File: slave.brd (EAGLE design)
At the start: 321.3 x 281.9 mm, 324 parts, among them J2 EB21A-06-D, J3 EB21A-06-D, J4 EB21A-06-D, J5 EB21A-06-D, J6 282837-9, J7 282837-9, J8 282837-9, J9 1715250000, Q1 DMN2056U-7, Q10 DMN2056U-7, Q11 DMN2056U-7, Q12 DMN2056U-7, Q13 DMN2056U-7, Q14 DMN2056U-7, Q15 DMN2056U-7, Q16 DMN2056U-7, Q17 DMN2056U-7, Q18 DMN2056U-7, Q19 DMN2056U-7, Q2 DMN2056U-7, Q20 DMN2056U-7, Q21 DMN2056U-7, Q22 DMN2056U-7, Q23 DMN2056U-7, Q24 DMN2056U-7, Q25 DMN2056U-7, Q26 DMN2056U-7, Q27 DMN2056U-7, Q28 DMN2056U-7, Q29 DMN2056U-7, Q3 DMN2056U-7, Q30 DMN2056U-7, Q31 DMN2056U-7, Q32 DMN2056U-7, Q33 DMN2056U-7, Q34 DMN2056U-7, Q35 DMN2056U-7, Q36 DMN2056U-7, Q37 DMN2056U-7, Q38 DMN2056U-7, Q39 DMN2056U-7, Q4 DMN2056U-7, Q40 DMN2056U-7, Q41 DMN2056U-7, Q42 DMN2056U-7, Q5 DMN2056U-7, Q6 DMG2301L-7, Q7 DMN2056U-7, Q8 DMN2056U-7, Q9 DMN2056U-7, U2 AP2112K-3.3TRG1, U3 MCP23008-E/P, U4 MCP23008-E/P, U5 MCP23008-E/P, U6 MC74HCT4851ADR2G, U7 MC74HCT4851ADR2G, U8 MC74HCT4851ADR2G, U9 MC74HCT4851ADR2G

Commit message: removed backup files, finalized board layoout
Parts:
- removed D10, D8, D9: B5819W SL, ML_library:DIODE_SOD-123
- removed PR_CS1, PR_CS10, PR_CS11, PR_CS12, PR_CS13, PR_CS14, PR_CS15, PR_CS16, PR_CS17, PR_CS18, PR_CS19, PR_CS2, PR_CS20, PR_CS3, PR_CS4, PR_CS5, PR_CS6, PR_CS7, PR_CS8, PR_CS9: ACS723LLCTR-10AU-T, ACS723LLCTR-10AU-T:SOIC127P600X175-8N
- removed Q6: DMG2301L-7, ML_library:SOT23
- removed R32: 1k, OPL_Resistor:R0402
- removed R33: 10k, OPL_Resistor:R0402
- removed U$1, U$2: PPTC151LFBN-RC, PPTC151LFBN-RC:PPTC151LFBN-RC
- added ESP_LEFT_HDR, ESP_RIGHT_HDR: PPTC151LFBN-RC, PPTC151LFBN-RC:PPTC151LFBN-RC
- added OA_CS, OGF_CS, OGL_CS, OGR_CS, OR_CS, PA_CS, PGF_CS, PGL_CS, PGR_CS, PR_CS, SA_CS, SGF_CS, SGL_CS, SGR_CS, SPA_CS, SPGF_CS, SPGL_CS, SPGR_CS, SPR_CS, SR_CS: ACS723LLCTR-10AU-T, ACS723LLCTR-10AU-T:SOIC127P600X175-8N
- moved CB39 298.0 mm to (-240.1, 39.6), turned to 270 degrees
- moved R55 279.9 mm to (-203.3, 24.4), turned to 180 degrees
- moved CB36 279.3 mm to (-58.8, 41.5), turned to 90 degrees
- moved CB38 279.3 mm to (-69.0, 41.5), turned to 90 degrees
- moved R52 279.2 mm to (-186.8, 24.4), turned to 180 degrees
- moved CB35 278.4 mm to (-55.0, 41.5), turned to 270 degrees
- moved CB37 278.4 mm to (-65.2, 41.5), turned to 270 degrees
- moved R58 276.3 mm to (-212.2, 24.4), turned to 180 degrees
- moved R57 275.6 mm to (-205.8, 24.4)
- moved R54 274.9 mm to (-189.3, 24.4)
- moved R56 274.6 mm to (-204.6, 28.2), turned to 90 degrees
- moved R53 273.9 mm to (-188.1, 28.2), turned to 90 degrees
- moved R61 272.8 mm to (-221.1, 24.4), turned to 180 degrees
- moved R60 272.2 mm to (-214.7, 24.4)
- moved R59 271.0 mm to (-213.5, 28.2), turned to 90 degrees
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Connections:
- removed net 3V3_F: Q6.P$3
- removed net N$10: D8.2, D9.2, R32.1
- removed net N$35: CB9.1, PR_CS5.5
- removed net N$47: CB21.1, PR_CS11.5
- removed net N$5: D10.2, Q6.P$2
- removed net N$59: CB33.1, PR_CS17.5
- removed net N$65: CB39.1, PR_CS20.5
- removed net PMOS_G: Q6.P$1, R32.2, R33.2
- removed net VBAT: D9.1
- removed net VUSB: D8.1
- new net N$13: CB9.1, PGR_CS.5
- new net N$14: CB21.1, SGR_CS.5
- new net N$16: CB33.1, OGR_CS.5
- new net N$17: CB39.1, SPGR_CS.5
- net +5V: now also OA_CS.6, OA_CS.8, OGF_CS.6, OGF_CS.8, OGL_CS.6, OGL_CS.8, OGR_CS.6, OGR_CS.8, OR_CS.6, OR_CS.8, PA_CS.6, PA_CS.8, PGF_CS.6, PGF_CS.8, PGL_CS.6, PGL_CS.8, PGR_CS.6, PGR_CS.8, PR_CS.6, PR_CS.8, SA_CS.6, SA_CS.8, SGF_CS.6, SGF_CS.8, SGL_CS.6, SGL_CS.8, SGR_CS.6, SGR_CS.8, SPA_CS.6, SPA_CS.8, SPGF_CS.6, SPGF_CS.8, SPGL_CS.6, SPGL_CS.8, SPGR_CS.6, SPGR_CS.8, SPR_CS.6, SPR_CS.8, SR_CS.6, SR_CS.8; no longer PR_CS1.6, PR_CS1.8, PR_CS10.6, PR_CS10.8, PR_CS11.6, PR_CS11.8, PR_CS12.6, PR_CS12.8, PR_CS13.6, PR_CS13.8, PR_CS14.6, PR_CS14.8, PR_CS15.6, PR_CS15.8, PR_CS16.6, PR_CS16.8, PR_CS17.6, PR_CS17.8, PR_CS18.6, PR_CS18.8, PR_CS19.6, PR_CS19.8, PR_CS2.6, PR_CS2.8, PR_CS20.6, PR_CS20.8, PR_CS3.6, PR_CS3.8, PR_CS4.6, PR_CS4.8, PR_CS5.6, PR_CS5.8, PR_CS6.6, PR_CS6.8, PR_CS7.6, PR_CS7.8, PR_CS8.6, PR_CS8.8, PR_CS9.6, PR_CS9.8
- net 3V3: now also ESP_RIGHT_HDR.P$15; no longer D10.1, U$2.P$15
- net CS_SEL0: now also ESP_RIGHT_HDR.P$6; no longer U$2.P$6
- net CS_SEL1: now also ESP_RIGHT_HDR.P$4; no longer U$2.P$4
- net CS_SEL2: now also ESP_RIGHT_HDR.P$3; no longer U$2.P$3
- net D23: now also ESP_RIGHT_HDR.P$1; no longer U$2.P$1
- net EN: now also ESP_LEFT_HDR.P$1; no longer U$1.P$1
- net GND: now also ESP_LEFT_HDR.P$14, ESP_RIGHT_HDR.P$14; no longer R33.1, U$1.P$14, U$2.P$14
- net I_OA: now also OA_CS.7; no longer PR_CS8.7
- net I_OGF: now also OGF_CS.7; no longer PR_CS9.7
- net I_OGL: now also OGL_CS.7; no longer PR_CS10.7
- net I_OGR: now also OGR_CS.7; no longer PR_CS11.7
- net I_OR: now also OR_CS.7; no longer PR_CS7.7
- net I_PA: now also PA_CS.7; no longer PR_CS12.7
- net I_PGF: now also PGF_CS.7; no longer PR_CS18.7
- net I_PGL: now also PGL_CS.7; no longer PR_CS19.7
- net I_PGR: now also PGR_CS.7; no longer PR_CS20.7
- net I_PR: now also PR_CS.7; no longer PR_CS6.7
- net I_SA: now also SA_CS.7; no longer PR_CS2.7
- net I_SGF: now also SGF_CS.7; no longer PR_CS3.7
- net I_SGL: now also SGL_CS.7; no longer PR_CS4.7
- net I_SGR: now also SGR_CS.7; no longer PR_CS5.7
- net I_SPA: now also SPA_CS.7; no longer PR_CS14.7
- net I_SPGF: now also SPGF_CS.7; no longer PR_CS15.7
- net I_SPGL: now also SPGL_CS.7; no longer PR_CS16.7
- net I_SPGR: now also SPGR_CS.7; no longer PR_CS17.7
- net I_SPR: now also SPR_CS.7; no longer PR_CS13.7
- net I_SR: now also SR_CS.7; no longer PR_CS1.7
- net N$29: now also SR_CS.5; no longer PR_CS1.5
- net N$31: now also SA_CS.5; no longer PR_CS2.5
- net N$33: now also SGF_CS.5; no longer PR_CS3.5
- net N$37: now also PR_CS.5; no longer PR_CS6.5
- net N$39: now also OR_CS.5; no longer PR_CS7.5
- net N$4: now also SGL_CS.5; no longer PR_CS4.5
- net N$41: now also OA_CS.5; no longer PR_CS8.5
- net N$43: now also OGF_CS.5; no longer PR_CS9.5
- net N$45: now also OGL_CS.5; no longer PR_CS10.5
- net N$49: now also PA_CS.5; no longer PR_CS12.5
- net N$51: now also SPR_CS.5; no longer PR_CS13.5
- net N$53: now also SPA_CS.5; no longer PR_CS14.5
- net N$55: now also SPGF_CS.5; no longer PR_CS15.5
- net N$57: now also SPGL_CS.5; no longer PR_CS16.5
- net N$61: now also PGF_CS.5; no longer PR_CS18.5
- net N$63: now also PGL_CS.5; no longer PR_CS19.5
- net OA_IP-: now also OA_CS.3, OA_CS.4; no longer PR_CS8.3, PR_CS8.4
- net OGF_IP-: now also OGF_CS.3, OGF_CS.4; no longer PR_CS9.3, PR_CS9.4
- net OGL_IP-: now also OGL_CS.3, OGL_CS.4; no longer PR_CS10.3, PR_CS10.4
- net OGR_IP-: now also OGR_CS.3, OGR_CS.4; no longer PR_CS11.3, PR_CS11.4
- net OR_IP-: now also OR_CS.3, OR_CS.4; no longer PR_CS7.3, PR_CS7.4
- net O_CURRENT: now also ESP_LEFT_HDR.P$5; no longer U$1.P$5
- net PA: now also ESP_LEFT_HDR.P$12; no longer U$1.P$12
- net PA_IP-: now also PA_CS.3, PA_CS.4; no longer PR_CS12.3, PR_CS12.4
- net PGF: now also ESP_LEFT_HDR.P$11; no longer U$1.P$11
- net PGF_IP-: now also PGF_CS.3, PGF_CS.4; no longer PR_CS18.3, PR_CS18.4
- net PGL: now also ESP_LEFT_HDR.P$10; no longer U$1.P$10
- net PGL_IP-: now also PGL_CS.3, PGL_CS.4; no longer PR_CS19.3, PR_CS19.4
- net PGR: now also ESP_LEFT_HDR.P$9; no longer U$1.P$9
- net PGR_IP-: now also PGR_CS.3, PGR_CS.4; no longer PR_CS20.3, PR_CS20.4
- net PR: now also ESP_LEFT_HDR.P$13; no longer U$1.P$13
- net PR_IP-: now also PR_CS.3, PR_CS.4; no longer PR_CS6.3, PR_CS6.4
- net P_CURRENT: now also ESP_LEFT_HDR.P$7; no longer U$1.P$7
- net SA: now also ESP_LEFT_HDR.P$3; no longer U$1.P$3
- net SA_IP-: now also SA_CS.3, SA_CS.4; no longer PR_CS2.3, PR_CS2.4
- net SCL: now also ESP_RIGHT_HDR.P$2; no longer U$2.P$2
- net SDA: now also ESP_RIGHT_HDR.P$5; no longer U$2.P$5
- net SGF: now also ESP_LEFT_HDR.P$2; no longer U$1.P$2
- net SGF_IP-: now also SGF_CS.3, SGF_CS.4; no longer PR_CS3.3, PR_CS3.4
- net SGL: now also ESP_RIGHT_HDR.P$13; no longer U$2.P$13
- net SGL_IP-: now also SGL_CS.3, SGL_CS.4; no longer PR_CS4.3, PR_CS4.4
- net SGR: now also ESP_RIGHT_HDR.P$12; no longer U$2.P$12
- net SGR_IP-: now also SGR_CS.3, SGR_CS.4; no longer PR_CS5.3, PR_CS5.4
- net SPA: now also ESP_RIGHT_HDR.P$10; no longer U$2.P$10
- net SPA_IP-: now also SPA_CS.3, SPA_CS.4; no longer PR_CS14.3, PR_CS14.4
- net SPGF: now also ESP_RIGHT_HDR.P$9; no longer U$2.P$9
- net SPGF_IP-: now also SPGF_CS.3, SPGF_CS.4; no longer PR_CS15.3, PR_CS15.4
- net SPGL: now also ESP_RIGHT_HDR.P$8; no longer U$2.P$8
- net SPGL_IP-: now also SPGL_CS.3, SPGL_CS.4; no longer PR_CS16.3, PR_CS16.4
- net SPGR: now also ESP_RIGHT_HDR.P$7; no longer U$2.P$7
- net SPGR_IP-: now also SPGR_CS.3, SPGR_CS.4; no longer PR_CS17.3, PR_CS17.4
- net SPR: now also ESP_RIGHT_HDR.P$11; no longer U$2.P$11
- net SPR_IP-: now also SPR_CS.3, SPR_CS.4; no longer PR_CS13.3, PR_CS13.4
- net SP_CURRENT: now also ESP_LEFT_HDR.P$4; no longer U$1.P$4
- net SR: now also ESP_LEFT_HDR.P$8; no longer U$1.P$8
- net SR_IP-: now also SR_CS.3, SR_CS.4; no longer PR_CS1.3, PR_CS1.4
- net S_CURRENT: now also ESP_LEFT_HDR.P$6; no longer U$1.P$6
- net VIN: now also OA_CS.1, OA_CS.2, OGF_CS.1, OGF_CS.2, OGL_CS.1, OGL_CS.2, OGR_CS.1, OGR_CS.2, OR_CS.1, OR_CS.2, PA_CS.1, PA_CS.2, PGF_CS.1, PGF_CS.2, PGL_CS.1, PGL_CS.2, PGR_CS.1, PGR_CS.2, PR_CS.1, PR_CS.2, SA_CS.1, SA_CS.2, SGF_CS.1, SGF_CS.2, SGL_CS.1, SGL_CS.2, SGR_CS.1, SGR_CS.2, SPA_CS.1, SPA_CS.2, SPGF_CS.1, SPGF_CS.2, SPGL_CS.1, SPGL_CS.2, SPGR_CS.1, SPGR_CS.2, SPR_CS.1, SPR_CS.2, SR_CS.1, SR_CS.2; no longer PR_CS1.1, PR_CS1.2, PR_CS10.1, PR_CS10.2, PR_CS11.1, PR_CS11.2, PR_CS12.1, PR_CS12.2, PR_CS13.1, PR_CS13.2, PR_CS14.1, PR_CS14.2, PR_CS15.1, PR_CS15.2, PR_CS16.1, PR_CS16.2, PR_CS17.1, PR_CS17.2, PR_CS18.1, PR_CS18.2, PR_CS19.1, PR_CS19.2, PR_CS2.1, PR_CS2.2, PR_CS20.1, PR_CS20.2, PR_CS3.1, PR_CS3.2, PR_CS4.1, PR_CS4.2, PR_CS5.1, PR_CS5.2, PR_CS6.1, PR_CS6.2, PR_CS7.1, PR_CS7.2, PR_CS8.1, PR_CS8.2, PR_CS9.1, PR_CS9.2
- net VIN_ESP: now also ESP_LEFT_HDR.P$15; no longer U$1.P$15
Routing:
- net GND: track 0.00 -> 953.3 mm, vias 0 -> 9
- net JP2: track 0.00 -> 883.3 mm, vias 0 -> 23
- net +5V: track 0.00 -> 862.8 mm, vias 0 -> 15
- net VIN: track 0.00 -> 771.2 mm, vias 0 -> 15
- net PLED_GND: track 0.00 -> 285.2 mm, vias 0 -> 3
- net CS_SEL0: track 0.00 -> 239.1 mm, vias 0 -> 7
- net CS_SEL2: track 0.00 -> 235.4 mm, vias 0 -> 5
- net CS_SEL1: track 0.00 -> 234.9 mm, vias 0 -> 7
- net SDA: track 0.00 -> 167.7 mm
- net SCL: track 0.00 -> 161.1 mm, vias 0 -> 2
- net PR: track 0.00 -> 125.9 mm, vias 0 -> 3
- net PGF: track 0.00 -> 125.5 mm, vias 0 -> 3
- net PGL: track 0.00 -> 124.7 mm, vias 0 -> 2
- net SR: track 0.00 -> 123.9 mm
- net EN: track 0.00 -> 123.5 mm
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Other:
- board size 321.3 x 281.9 mm -> 221.8 x 119.2 mm

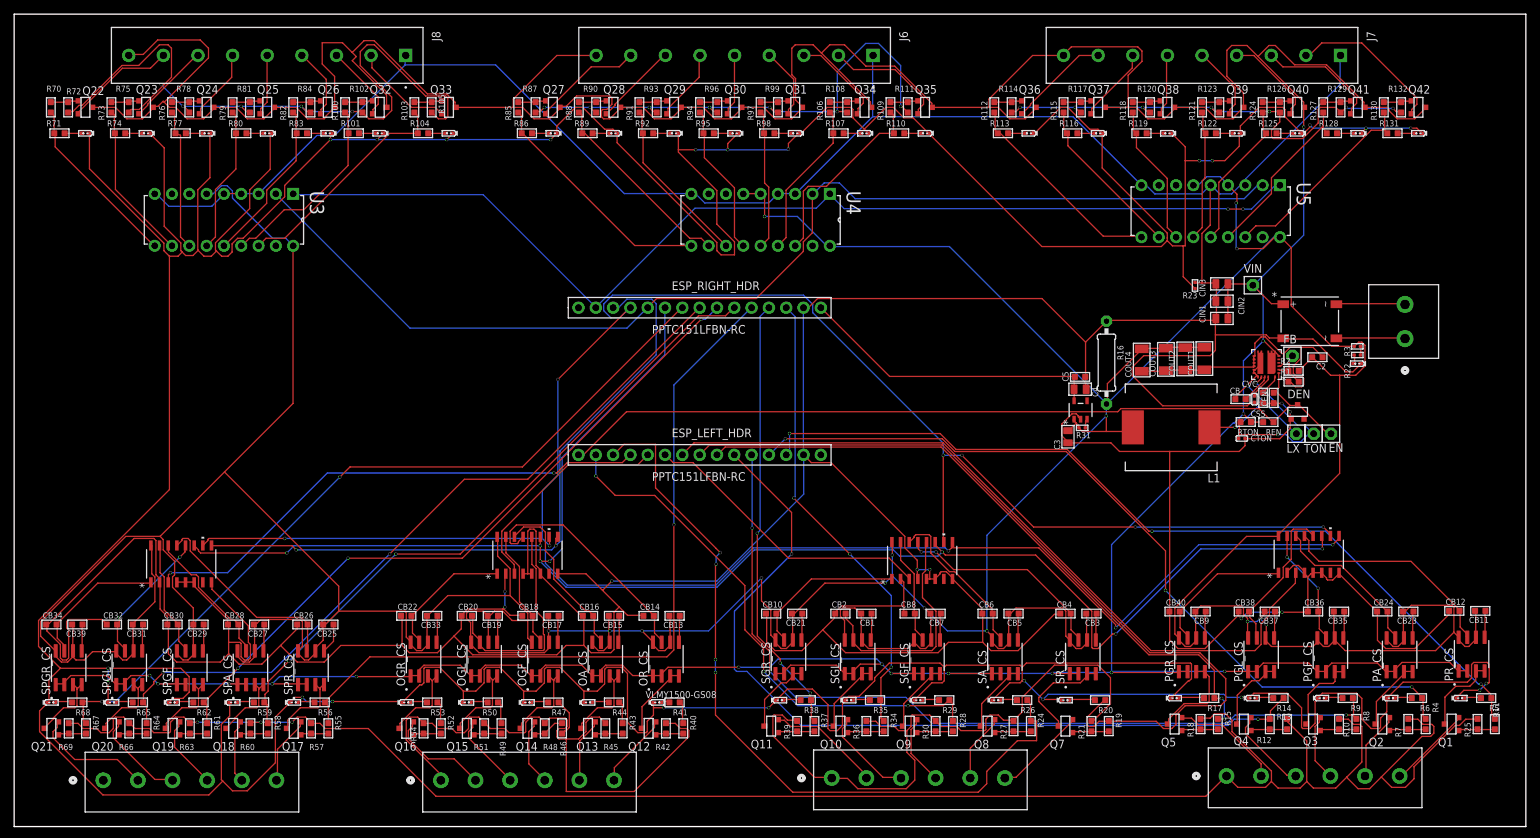
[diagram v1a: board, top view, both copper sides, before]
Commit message: changed header, but clearance issues
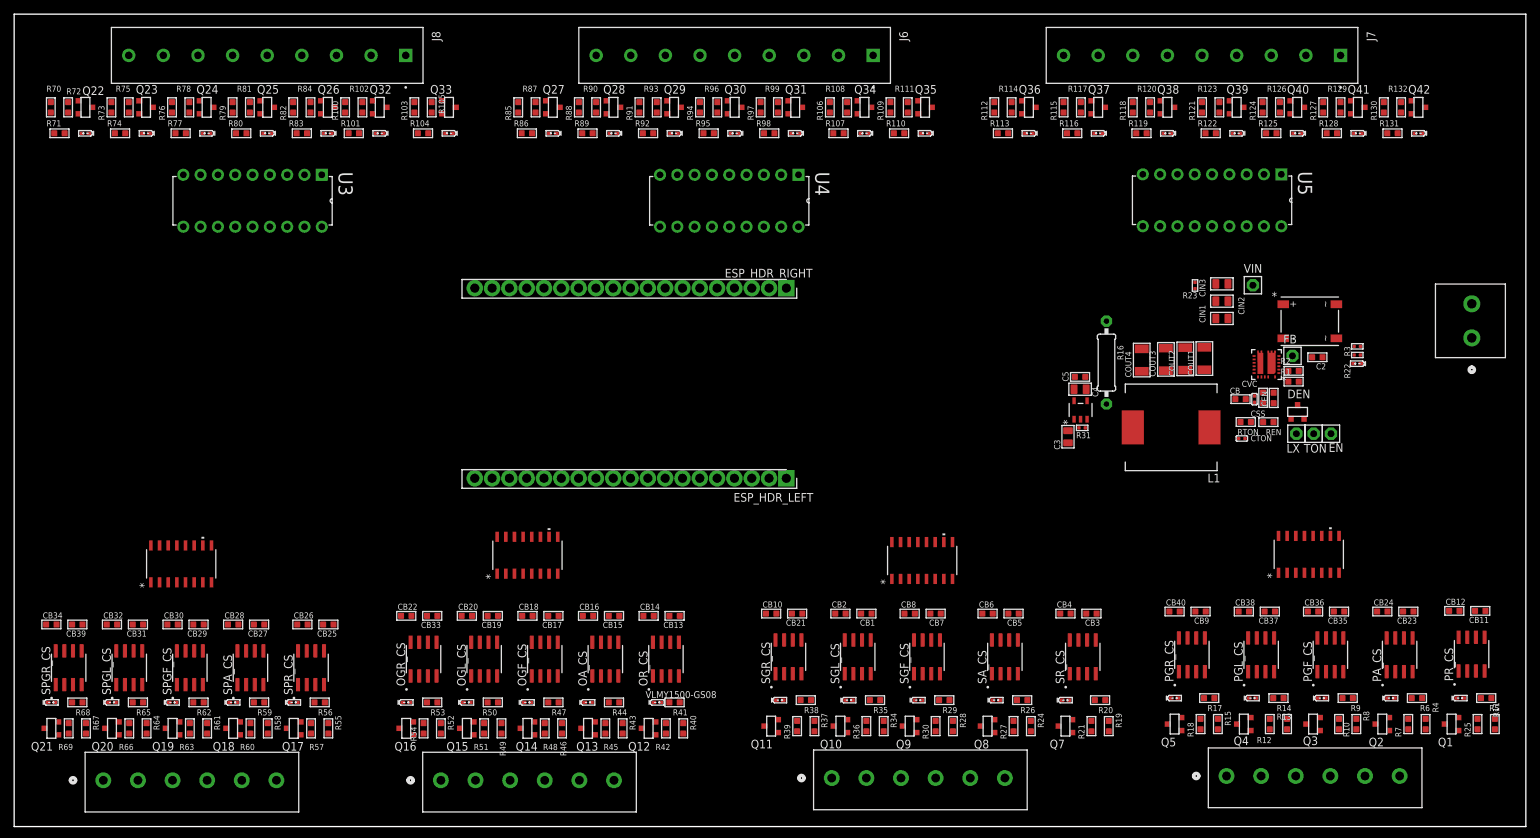
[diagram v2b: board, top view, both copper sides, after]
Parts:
- removed ESP_LEFT_HDR, ESP_RIGHT_HDR: PPTC151LFBN-RC, PPTC151LFBN-RC:PPTC151LFBN-RC
- added ESP_HDR_LEFT, ESP_HDR_RIGHT: PPTC191LFBN-RC, PPTC191LFBN-RC:RHDR19W80P0X254_1X19_4876X254X
- moved J9 9.80 mm to (-35.5, 81.7)
- moved U4 5.39 mm to (-154.6, 98.0)
- moved U3 5.05 mm to (-224.6, 98.0)
- moved U5 1.61 mm to (-83.8, 98.1)
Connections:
- removed net D23: ESP_RIGHT_HDR.P$1
- removed net N$13: CB9.1, PGR_CS.5
- removed net N$14: CB21.1, SGR_CS.5
- removed net N$16: CB33.1, OGR_CS.5
- removed net N$17: CB39.1, SPGR_CS.5
- removed net N$29: CB3.1, SR_CS.5
- removed net N$31: CB5.1, SA_CS.5
- removed net N$33: CB7.1, SGF_CS.5
- removed net N$37: CB11.1, PR_CS.5
- removed net N$39: CB13.1, OR_CS.5
- removed net N$4: CB1.1, SGL_CS.5
- removed net N$41: CB15.1, OA_CS.5
- removed net N$43: CB17.1, OGF_CS.5
- removed net N$45: CB19.1, OGL_CS.5
- removed net N$49: CB23.1, PA_CS.5
- removed net N$51: CB25.1, SPR_CS.5
- removed net N$53: CB27.1, SPA_CS.5
- removed net N$55: CB29.1, SPGF_CS.5
- removed net N$57: CB31.1, SPGL_CS.5
- removed net N$61: CB35.1, PGF_CS.5
- removed net N$63: CB37.1, PGL_CS.5
- removed net VIN_ESP: ESP_LEFT_HDR.P$15
- new net 5V0: ESP_HDR_LEFT.1
- new net ESP_EN: ESP_HDR_LEFT.18
- new net GPIO1: ESP_HDR_RIGHT.16
- new net GPIO10: ESP_HDR_LEFT.3
- new net GPIO11: ESP_HDR_LEFT.2
- new net GPIO3: ESP_HDR_RIGHT.15
- new net GPIO6: ESP_HDR_RIGHT.1
- new net GPIO7: ESP_HDR_RIGHT.2
- new net GPIO8: ESP_HDR_RIGHT.3
- new net GPIO9: ESP_HDR_LEFT.4
- net 3V3: now also ESP_HDR_LEFT.19; no longer ESP_RIGHT_HDR.P$15
- net CS_SEL0: now also ESP_HDR_LEFT.5; no longer ESP_RIGHT_HDR.P$6
- net CS_SEL1: now also ESP_HDR_LEFT.7; no longer ESP_RIGHT_HDR.P$4
- net CS_SEL2: now also ESP_HDR_LEFT.8; no longer ESP_RIGHT_HDR.P$3
- net EN: no longer ESP_LEFT_HDR.P$1
- net GND: now also CB1.1, CB11.1, CB13.1, CB15.1, CB17.1, CB19.1, CB21.1, CB23.1, CB25.1, CB27.1, CB29.1, CB3.1, CB31.1, CB33.1, CB35.1, CB37.1, CB39.1, CB5.1, CB7.1, CB9.1, ESP_HDR_LEFT.6, ESP_HDR_RIGHT.13, ESP_HDR_RIGHT.19, OA_CS.5, OGF_CS.5, OGL_CS.5, OGR_CS.5, OR_CS.5, PA_CS.5, PGF_CS.5, PGL_CS.5, PGR_CS.5, PR_CS.5, SA_CS.5, SGF_CS.5, SGL_CS.5, SGR_CS.5, SPA_CS.5, SPGF_CS.5, SPGL_CS.5, SPGR_CS.5, SPR_CS.5, SR_CS.5; no longer ESP_LEFT_HDR.P$14, ESP_RIGHT_HDR.P$14
- net O_CURRENT: now also ESP_HDR_LEFT.16; no longer ESP_LEFT_HDR.P$5
- net PA: now also ESP_HDR_LEFT.10; no longer ESP_LEFT_HDR.P$12
- net PGF: now also ESP_HDR_LEFT.11; no longer ESP_LEFT_HDR.P$11
- net PGL: now also ESP_HDR_LEFT.12; no longer ESP_LEFT_HDR.P$10
- net PGR: now also ESP_HDR_LEFT.13; no longer ESP_LEFT_HDR.P$9
- net PR: now also ESP_HDR_LEFT.9; no longer ESP_LEFT_HDR.P$13
- net P_CURRENT: now also ESP_HDR_LEFT.14; no longer ESP_LEFT_HDR.P$7
- net SA: now also ESP_HDR_RIGHT.9; no longer ESP_LEFT_HDR.P$3
- net SCL: now also ESP_HDR_RIGHT.17; no longer ESP_RIGHT_HDR.P$2
- net SDA: now also ESP_HDR_RIGHT.14; no longer ESP_RIGHT_HDR.P$5
- net SGF: now also ESP_HDR_RIGHT.10; no longer ESP_LEFT_HDR.P$2
- net SGL: now also ESP_HDR_RIGHT.11; no longer ESP_RIGHT_HDR.P$13
- net SGR: now also ESP_HDR_RIGHT.12; no longer ESP_RIGHT_HDR.P$12
- net SPA: now also ESP_HDR_RIGHT.5; no longer ESP_RIGHT_HDR.P$10
- net SPGF: now also ESP_HDR_RIGHT.6; no longer ESP_RIGHT_HDR.P$9
- net SPGL: now also ESP_HDR_RIGHT.7; no longer ESP_RIGHT_HDR.P$8
- net SPGR: now also ESP_HDR_RIGHT.8; no longer ESP_RIGHT_HDR.P$7
- net SPR: now also ESP_HDR_RIGHT.4; no longer ESP_RIGHT_HDR.P$11
- net SP_CURRENT: now also ESP_HDR_LEFT.17; no longer ESP_LEFT_HDR.P$4
- net SR: now also ESP_HDR_RIGHT.18; no longer ESP_LEFT_HDR.P$8
- net S_CURRENT: now also ESP_HDR_LEFT.15; no longer ESP_LEFT_HDR.P$6
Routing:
- net GND: track 953.3 -> 0.00 mm, vias 9 -> 0
- net JP2: track 883.3 -> 0.00 mm, vias 23 -> 0
- net +5V: track 862.8 -> 0.00 mm, vias 15 -> 0
- net VIN: track 771.2 -> 0.00 mm, vias 15 -> 0
- net PLED_GND: track 285.2 -> 0.00 mm, vias 3 -> 0
- net CS_SEL0: track 239.1 -> 0.00 mm, vias 7 -> 0
- net CS_SEL2: track 235.4 -> 0.00 mm, vias 5 -> 0
- net CS_SEL1: track 234.9 -> 0.00 mm, vias 7 -> 0
- net SDA: track 167.7 -> 0.00 mm
- net SCL: track 161.1 -> 0.00 mm, vias 2 -> 0
- net PR: track 125.9 -> 0.00 mm, vias 3 -> 0
- net PGF: track 125.5 -> 0.00 mm, vias 3 -> 0
- net PGL: track 124.7 -> 0.00 mm, vias 2 -> 0
- net SR: track 123.9 -> 0.00 mm
- net EN: track 123.5 -> 0.00 mm
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
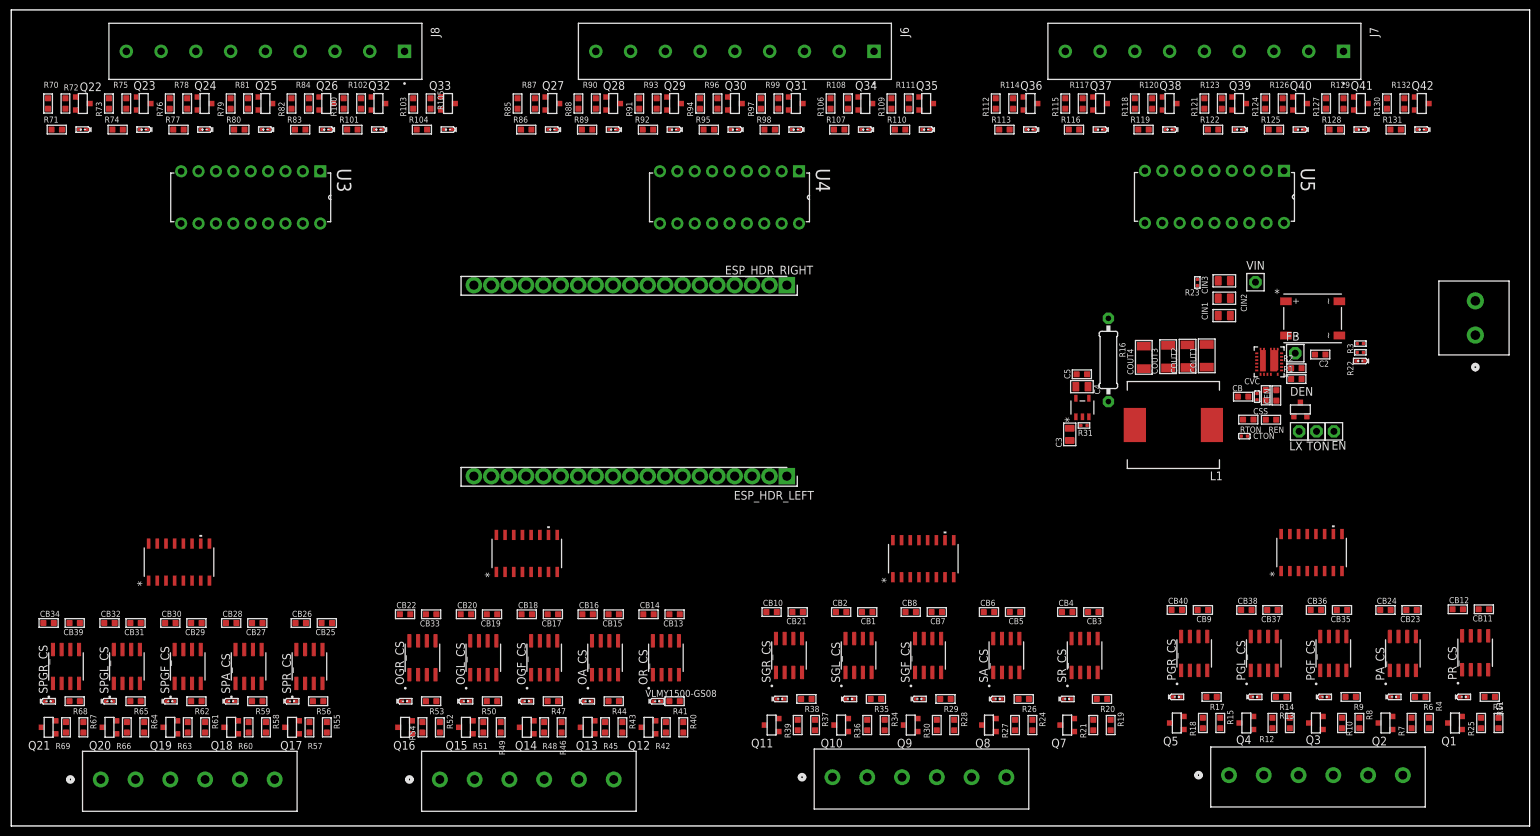
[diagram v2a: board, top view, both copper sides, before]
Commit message: fixed trace widths of lamp mos and current sensor power traces
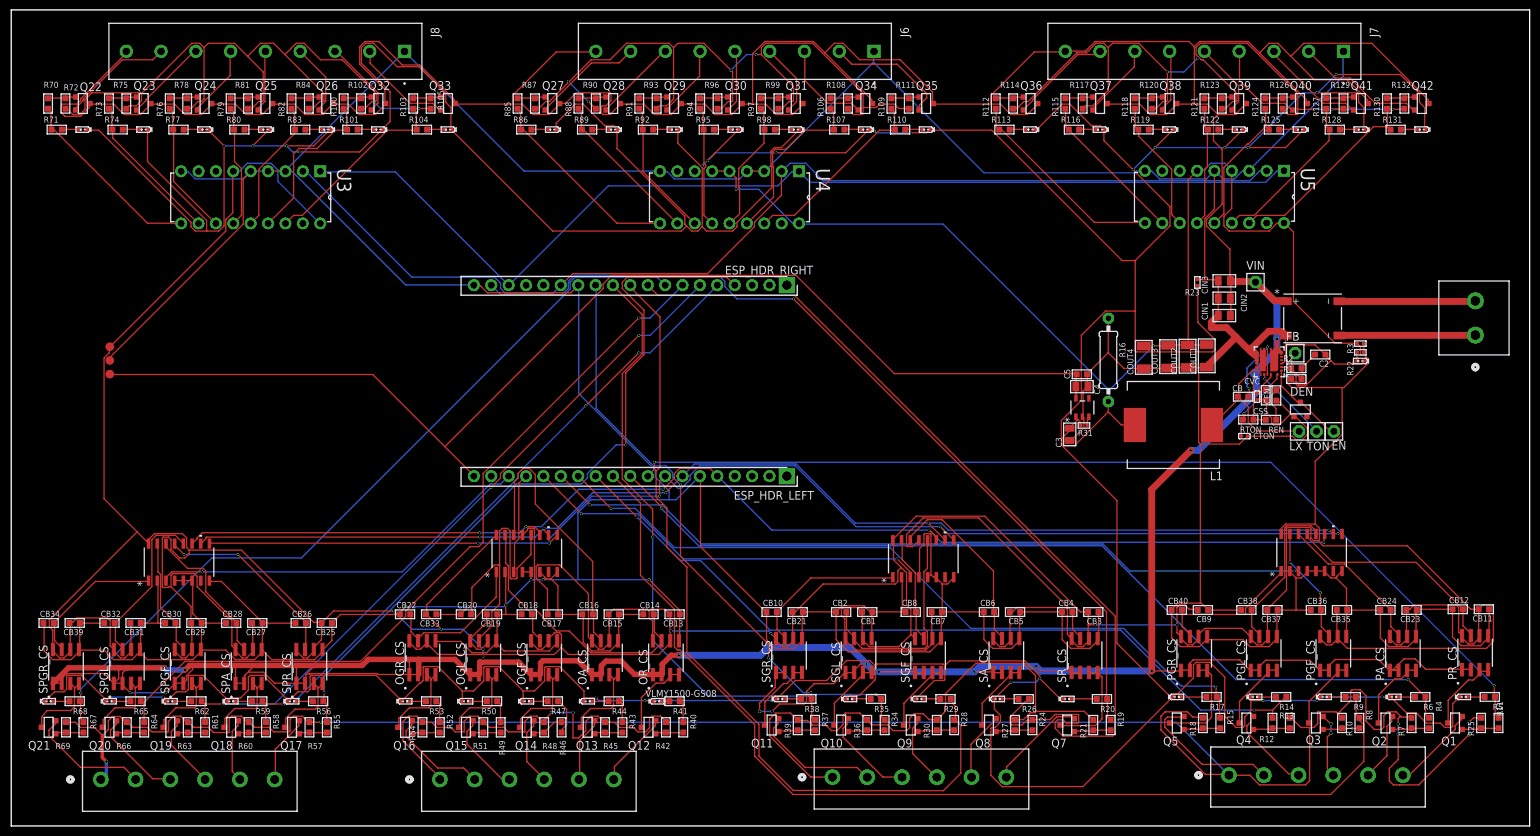
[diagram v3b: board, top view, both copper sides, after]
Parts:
- added TP1, TP4, TP5: TPB1,27, testpad:B1,27
- RTON: value 1.5M -> 781.25k
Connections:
- removed net N$6: C2.1, COUT1.1, COUT2.1, COUT3.1, COUT4.1, R1.2, REG.12, REG.13, REG.14, REG.15, REG.3
- removed net SPLED_GND: J5.1
- net +5V: now also TP1.TP
- net 3V3: now also TP5.TP
- net GND: now also C2.1, COUT1.1, COUT2.1, COUT3.1, COUT4.1, R1.2, REG.12, REG.13, REG.14, REG.15, REG.3, TP4.TP
- net PLED_GND: now also J5.1
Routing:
- net GND: track 0.00 -> 1052.2 mm, vias 0 -> 6
- net +5V: track 0.00 -> 951.1 mm, vias 0 -> 10
- net JP2: track 0.00 -> 875.4 mm, vias 0 -> 25
- net VIN: track 0.00 -> 849.6 mm, vias 0 -> 15
- net PLED_GND: track 0.00 -> 293.3 mm, vias 0 -> 6
- net CS_SEL2: track 0.00 -> 182.2 mm, vias 0 -> 5
- net CS_SEL0: track 0.00 -> 180.8 mm, vias 0 -> 5
- net CS_SEL1: track 0.00 -> 179.3 mm, vias 0 -> 5
- net 3V3: track 0.00 -> 172.0 mm
- net SDA: track 0.00 -> 160.5 mm
- net SCL: track 0.00 -> 156.0 mm
- net PGF: track 0.00 -> 152.9 mm
- net PR: track 0.00 -> 143.5 mm, vias 0 -> 2
- net SA: track 0.00 -> 136.2 mm
- net PA: track 0.00 -> 132.9 mm, vias 0 -> 2
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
